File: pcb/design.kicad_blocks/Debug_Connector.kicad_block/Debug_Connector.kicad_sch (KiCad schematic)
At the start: 1 part, among them J5 Debug

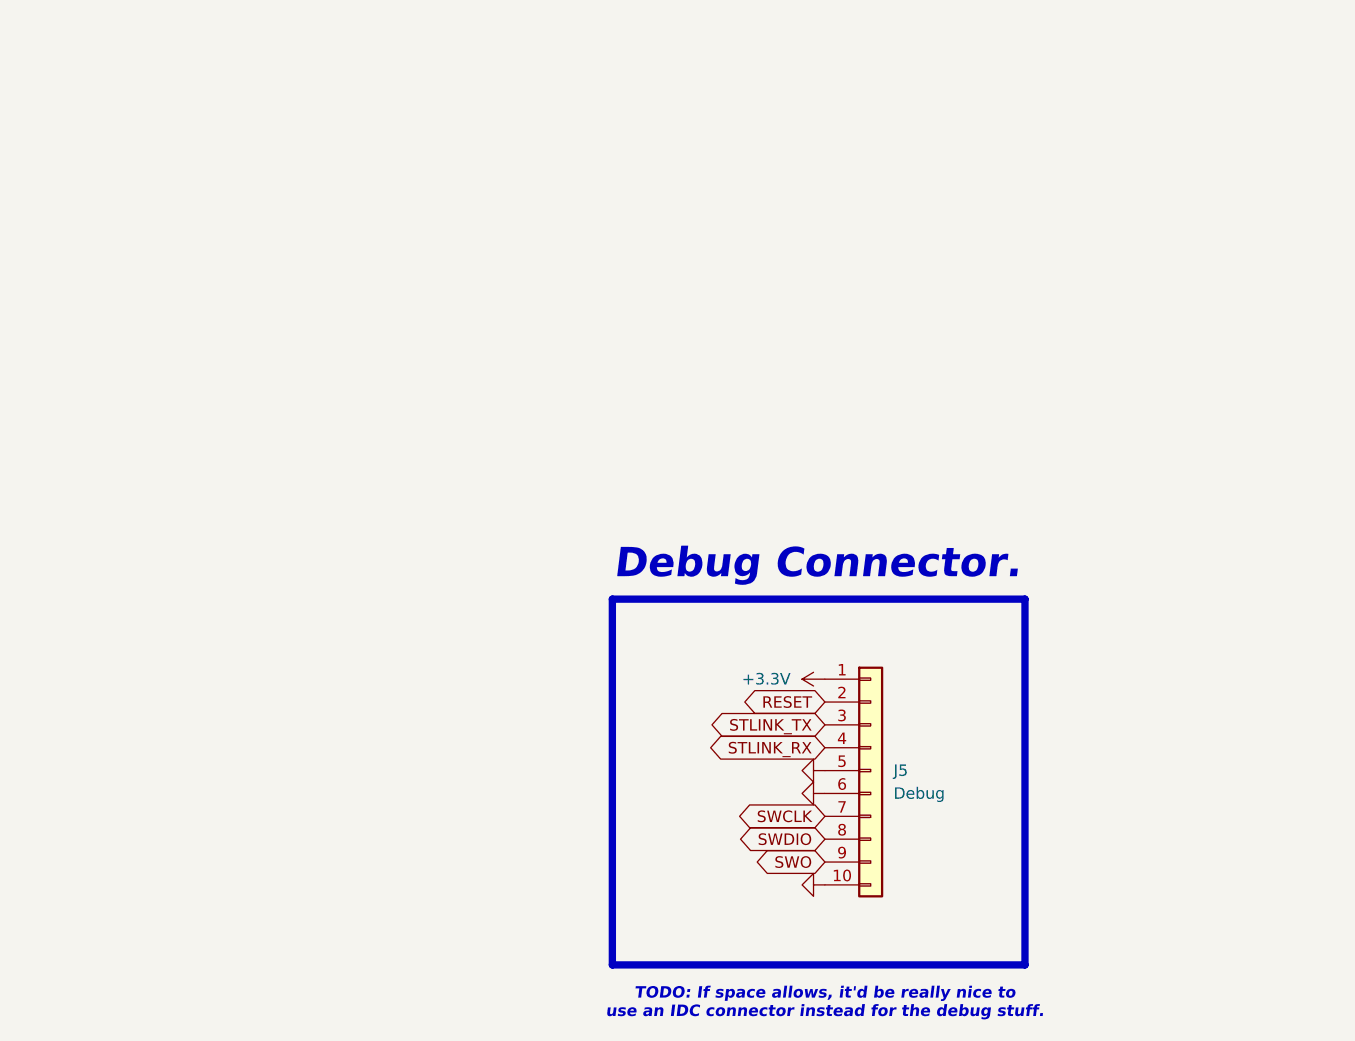
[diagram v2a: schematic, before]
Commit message: Made some net-names of debug connector lowercase.
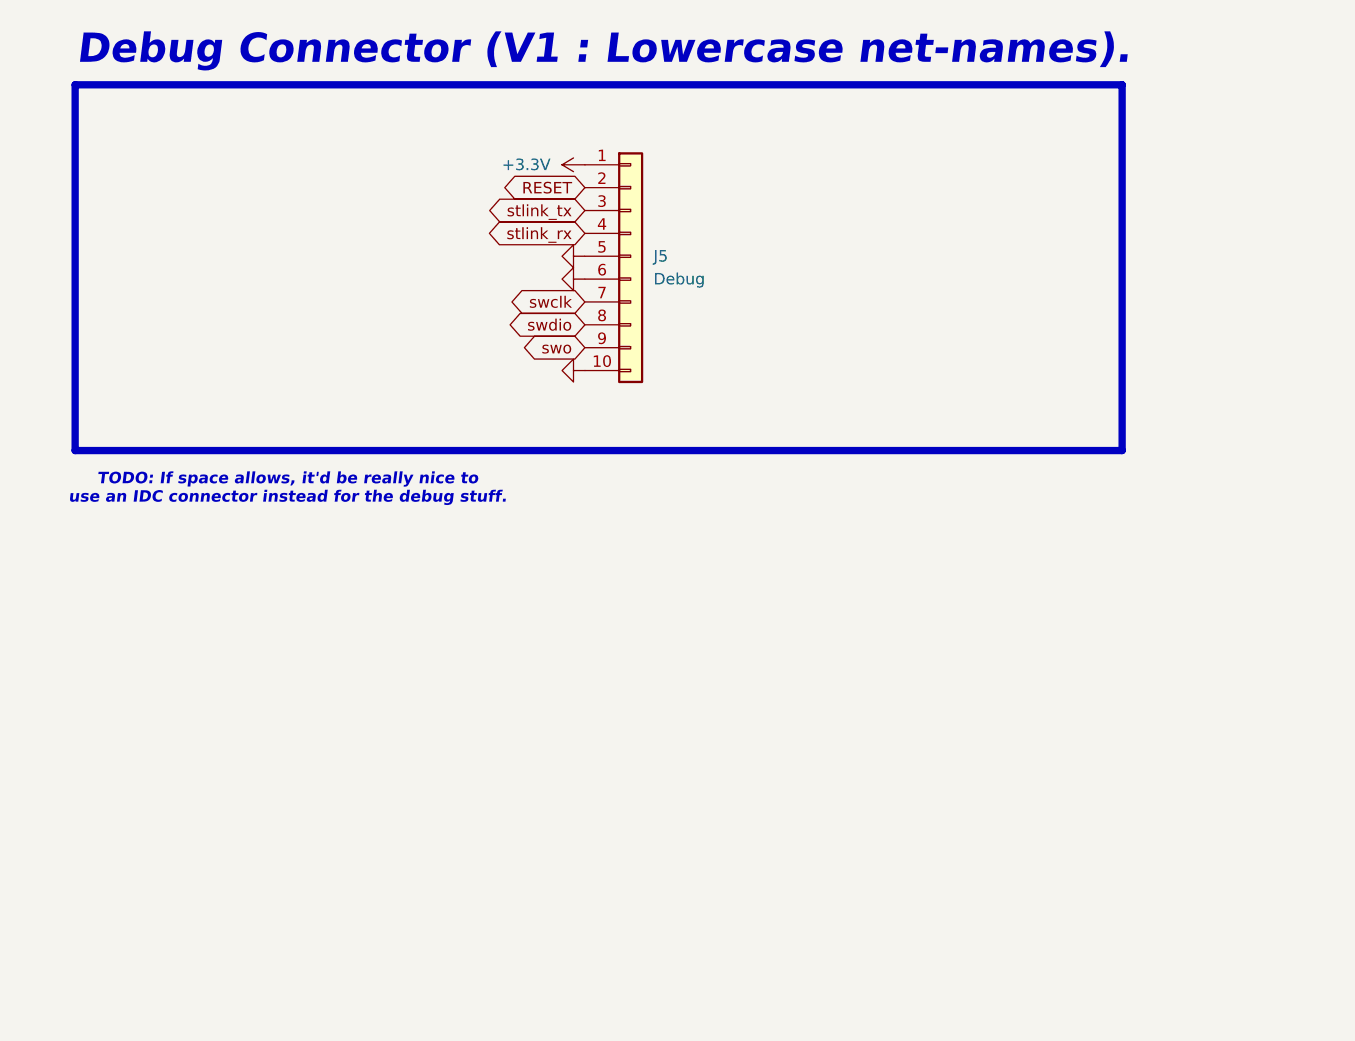
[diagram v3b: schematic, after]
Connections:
- net STLINK_RX renamed stlink_rx
- net STLINK_TX renamed stlink_tx
- net SWCLK renamed swclk
- net SWDIO renamed swdio
- net SWO renamed swo
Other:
- note added: "Debug Connector (V1 : Lowercase net-names)."
- note removed: "Debug Connector."
- moved on the sheet: J5
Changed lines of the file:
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@@
 	(paper "A4")
 	(rectangle
-		(start 500.888 267.97)
-		(end 546.735 308.61)
+		(start 441.198 210.82)
+		(end 557.53 251.46)
 		(stroke
 			(width 0.8128)
@@
 		)
 	)
-	(text "Debug Connector."
-		(exclude_from_sim no)
-		(at 501.015 266.065 0)
+	(text "Debug Connector (V1 : Lowercase net-names)."
+		(exclude_from_sim no)
+		(at 441.325 208.915 0)
 		(effects
 			(font
@@
 	(text "TODO: If space allows, it'd be really nice to\nuse an IDC connector instead for the debug stuff."
 		(exclude_from_sim no)
-		(at 524.51 312.928 0)
+		(at 464.82 255.778 0)
 		(effects
 			(font
@@
 		)
 	)
-	(global_label "SWO"
-		(shape bidirectional)
-		(at 524.51 297.18 180)
-		(fields_autoplaced yes)
-		(effects
-			(font
-				(size 1.27 1.27)
-			)
-			(justify right)
-		)
-		(property "Intersheetrefs" "${INTERSHEET_REFS}"
-			(at 516.4221 297.18 0)
+	(global_label "swo"
+		(shape bidirectional)
+		(at 497.84 240.03 180)
+		(fields_autoplaced yes)
+		(effects
+			(font
+				(size 1.27 1.27)
+			)
+			(justify right)
+		)
+		(property "Intersheetrefs" "${INTERSHEET_REFS}"
+			(at 490.2359 240.03 0)
 			(effects
 				(font
@@
 	(global_label "RESET"
 		(shape bidirectional)
-		(at 524.51 279.4 180)
-		(fields_autoplaced yes)
-		(effects
-			(font
-				(size 1.27 1.27)
-			)
-			(justify right)
-		)
-		(property "Intersheetrefs" "${INTERSHEET_REFS}"
-			(at 514.6684 279.4 0)
-			(effects
-				(font
-					(size 1.27 1.27)
-				)
-				(justify right)
-				(hide yes)
-			)
-		)
-	)
-	(global_label "SWCLK"
-		(shape bidirectional)
-		(at 524.51 292.1 180)
-		(fields_autoplaced yes)
-		(effects
-			(font
-				(size 1.27 1.27)
-			)
-			(justify right)
-		)
-		(property "Intersheetrefs" "${INTERSHEET_REFS}"
-			(at 514.1845 292.1 0)
-			(effects
-				(font
-					(size 1.27 1.27)
-				)
-				(justify right)
-				(hide yes)
-			)
-		)
-	)
-	(global_label "STLINK_TX"
-		(shape bidirectional)
-		(at 524.51 281.94 180)
-		(fields_autoplaced yes)
-		(effects
-			(font
-				(size 1.27 1.27)
-			)
-			(justify right)
-		)
-		(property "Intersheetrefs" "${INTERSHEET_REFS}"
-			(at 510.8583 281.94 0)
-			(effects
-				(font
-					(size 1.27 1.27)
-				)
-				(justify right)
-				(hide yes)
-			)
-		)
-	)
-	(global_label "SWDIO"
-		(shape bidirectional)
-		(at 524.51 294.64 180)
-		(fields_autoplaced yes)
-		(effects
-			(font
-				(size 1.27 1.27)
-			)
-			(justify right)
-		)
-		(property "Intersheetrefs" "${INTERSHEET_REFS}"
-			(at 514.5473 294.64 0)
-			(effects
-				(font
-					(size 1.27 1.27)
-				)
-				(justify right)
-				(hide yes)
-			)
-		)
-	)
-	(global_label "STLINK_RX"
-		(shape bidirectional)
-		(at 524.51 284.48 180)
-		(fields_autoplaced yes)
-		(effects
-			(font
-				(size 1.27 1.27)
-			)
-			(justify right)
-		)
-		(property "Intersheetrefs" "${INTERSHEET_REFS}"
-			(at 510.5559 284.48 0)
+		(at 497.84 222.25 180)
+		(fields_autoplaced yes)
+		(effects
+			(font
+				(size 1.27 1.27)
+			)
+			(justify right)
+		)
+		(property "Intersheetrefs" "${INTERSHEET_REFS}"
+			(at 487.9984 222.25 0)
+			(effects
+				(font
+					(size 1.27 1.27)
+				)
+				(justify right)
+				(hide yes)
+			)
+		)
+	)
+	(global_label "swclk"
+		(shape bidirectional)
+		(at 497.84 234.95 180)
+		(fields_autoplaced yes)
+		(effects
+			(font
+				(size 1.27 1.27)
+			)
+			(justify right)
+		)
+		(property "Intersheetrefs" "${INTERSHEET_REFS}"
+			(at 488.603 234.95 0)
+			(effects
+				(font
+					(size 1.27 1.27)
+				)
+				(justify right)
+				(hide yes)
+			)
+		)
+	)
+	(global_label "stlink_tx"
+		(shape bidirectional)
+		(at 497.84 224.79 180)
+		(fields_autoplaced yes)
+		(effects
+			(font
+				(size 1.27 1.27)
+			)
+			(justify right)
+		)
+		(property "Intersheetrefs" "${INTERSHEET_REFS}"
+			(at 485.8212 224.79 0)
+			(effects
+				(font
+					(size 1.27 1.27)
+				)
+				(justify right)
+				(hide yes)
+			)
+		)
+	)
+	(global_label "swdio"
+		(shape bidirectional)
+		(at 497.84 237.49 180)
+		(fields_autoplaced yes)
+		(effects
+			(font
+				(size 1.27 1.27)
+			)
+			(justify right)
+		)
+		(property "Intersheetrefs" "${INTERSHEET_REFS}"
+			(at 488.4821 237.49 0)
+			(effects
+				(font
+					(size 1.27 1.27)
+				)
+				(justify right)
+				(hide yes)
+			)
+		)
+	)
+	(global_label "stlink_rx"
+		(shape bidirectional)
+		(at 497.84 227.33 180)
+		(fields_autoplaced yes)
+		(effects
+			(font
+				(size 1.27 1.27)
+			)
+			(justify right)
+		)
+		(property "Intersheetrefs" "${INTERSHEET_REFS}"
+			(at 485.7607 227.33 0)
 			(effects
 				(font
@@
 	(symbol
 		(lib_id "power:+3.3V")
-		(at 524.51 276.86 90)
+		(at 497.84 219.71 90)
 		(unit 1)
 		(exclude_from_sim no)
@@
 		(fields_autoplaced yes)
 		(property "Reference" "#PWR012"
-			(at 528.32 276.86 0)
+			(at 501.65 219.71 0)
 			(effects
 				(font
@@
 		)
 		(property "Value" "+3.3V"
-			(at 520.7 276.8599 90)
+			(at 494.03 219.7099 90)
 			(effects
 				(font
@@
 		)
 		(property "Footprint" ""
-			(at 524.51 276.86 0)
+			(at 497.84 219.71 0)
 			(effects
 				(font
@@
 		)
 		(property "Datasheet" ""
-			(at 524.51 276.86 0)
+			(at 497.84 219.71 0)
 			(effects
 				(font
@@
 		)
 		(property "Description" "Power symbol creates a global label with name \"+3.3V\""
-			(at 524.51 276.86 0)
+			(at 497.84 219.71 0)
 			(effects
 				(font
@@
 	(symbol
 		(lib_id "Connector_Generic:Conn_01x10")
-		(at 529.59 287.02 0)
+		(at 502.92 229.87 0)
 		(unit 1)
 		(exclude_from_sim no)
@@
 		(fields_autoplaced yes)
 		(property "Reference" "J5"
-			(at 532.13 287.0199 0)
+			(at 505.46 229.8699 0)
 			(effects
 				(font
@@
 		)
 		(property "Value" "Debug"
-			(at 532.13 289.5599 0)
+			(at 505.46 232.4099 0)
 			(effects
 				(font
@@
 		)
 		(property "Footprint" "pcb:Molex_PicoBlade_53047-1010_1x10_P1.25mm_Vertical"
-			(at 529.59 287.02 0)
+			(at 502.92 229.87 0)
 			(effects
 				(font
@@
 		)
 		(property "Datasheet" "~"
-			(at 529.59 287.02 0)
+			(at 502.92 229.87 0)
 			(effects
 				(font
@@
 		)
 		(property "Description" "Generic connector, single row, 01x10, script generated (kicad-library-utils/schlib/autogen/connector/)"
-			(at 529.59 287.02 0)
+			(at 502.92 229.87 0)
 			(effects
 				(font
@@
 	(symbol
 		(lib_id "power:GND")
-		(at 524.51 299.72 270)
+		(at 497.84 242.57 270)
 		(mirror x)
 		(unit 1)
@@
 		(fields_autoplaced yes)
 		(property "Reference" "#PWR017"
-			(at 518.16 299.72 0)
+			(at 491.49 242.57 0)
 			(effects
 				(font
@@
 		)
 		(property "Value" "GND"
-			(at 520.7 299.7199 90)
+			(at 494.03 242.5699 90)
 			(effects
 				(font
@@
 		)
 		(property "Footprint" ""
-			(at 524.51 299.72 0)
+			(at 497.84 242.57 0)
 			(effects
 				(font
@@
 		)
 		(property "Datasheet" ""
-			(at 524.51 299.72 0)
+			(at 497.84 242.57 0)
 			(effects
 				(font
@@
 		)
 		(property "Description" "Power symbol creates a global label with name \"GND\" , ground"
-			(at 524.51 299.72 0)
+			(at 497.84 242.57 0)
 			(effects
 				(font
@@
 	(symbol
 		(lib_id "power:GND")
-		(at 524.51 287.02 270)
+		(at 497.84 229.87 270)
 		(unit 1)
 		(exclude_from_sim no)
@@
 		(fields_autoplaced yes)
 		(property "Reference" "#PWR013"
-			(at 518.16 287.02 0)
+			(at 491.49 229.87 0)
 			(effects
 				(font
@@
 		)
 		(property "Value" "GND"
-			(at 520.7 287.0201 90)
+			(at 494.03 229.8701 90)
 			(effects
 				(font
@@
 		)
 		(property "Footprint" ""
-			(at 524.51 287.02 0)
+			(at 497.84 229.87 0)
 			(effects
 				(font
@@
 		)
 		(property "Datasheet" ""
-			(at 524.51 287.02 0)
+			(at 497.84 229.87 0)
 			(effects
 				(font
@@
 		)
 		(property "Description" "Power symbol creates a global label with name \"GND\" , ground"
-			(at 524.51 287.02 0)
+			(at 497.84 229.87 0)
 			(effects
 				(font
@@
 	(symbol
 		(lib_id "power:GND")
-		(at 524.51 289.56 270)
+		(at 497.84 232.41 270)
 		(mirror x)
 		(unit 1)
@@
 		(fields_autoplaced yes)
 		(property "Reference" "#PWR016"
-			(at 518.16 289.56 0)
+			(at 491.49 232.41 0)
 			(effects
 				(font
@@
 		)
 		(property "Value" "GND"
-			(at 520.7 289.5599 90)
+			(at 494.03 232.4099 90)
 			(effects
 				(font
@@
 		)
 		(property "Footprint" ""
-			(at 524.51 289.56 0)
+			(at 497.84 232.41 0)
 			(effects
 				(font
@@
 		)
 		(property "Datasheet" ""
-			(at 524.51 289.56 0)
+			(at 497.84 232.41 0)
 			(effects
 				(font
@@
 		)
 		(property "Description" "Power symbol creates a global label with name \"GND\" , ground"
-			(at 524.51 289.56 0)
-			(effects
-				(font
+			(at 497.84 232.41 0)
+			(effects
+				(font
